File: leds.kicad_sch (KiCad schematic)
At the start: 32 parts

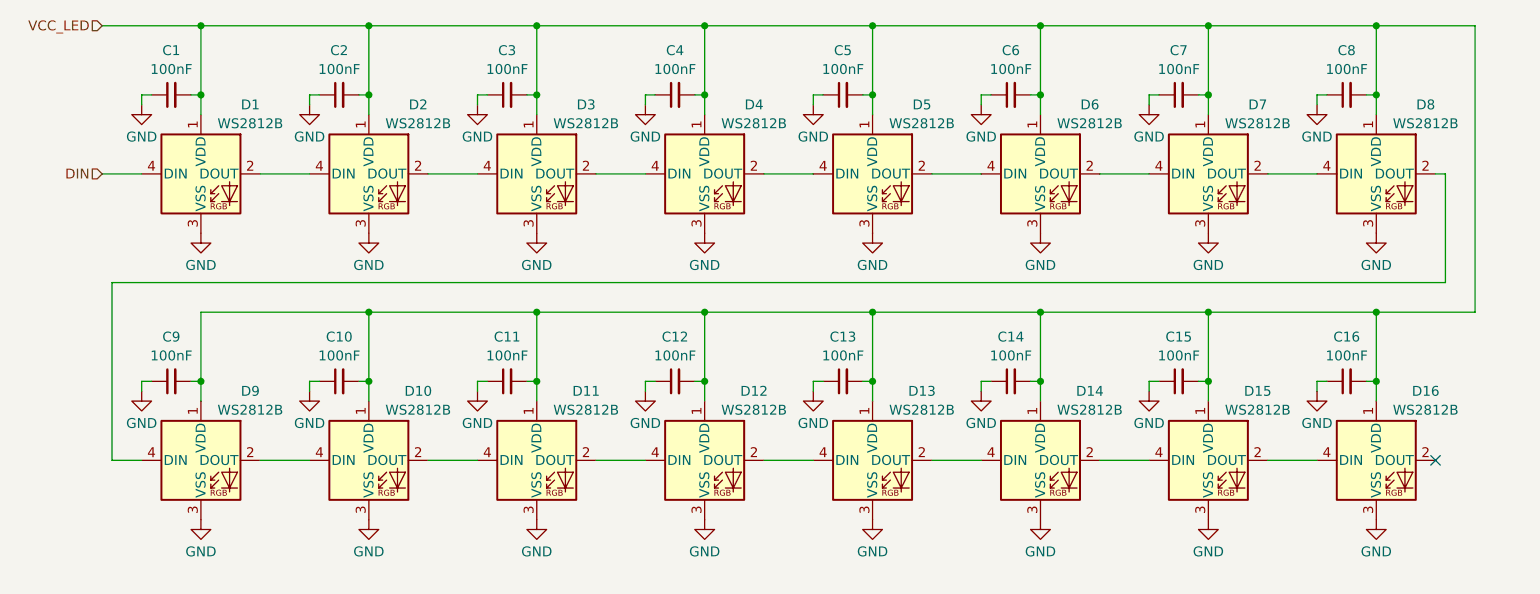
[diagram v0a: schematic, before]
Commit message: Finish rough layout
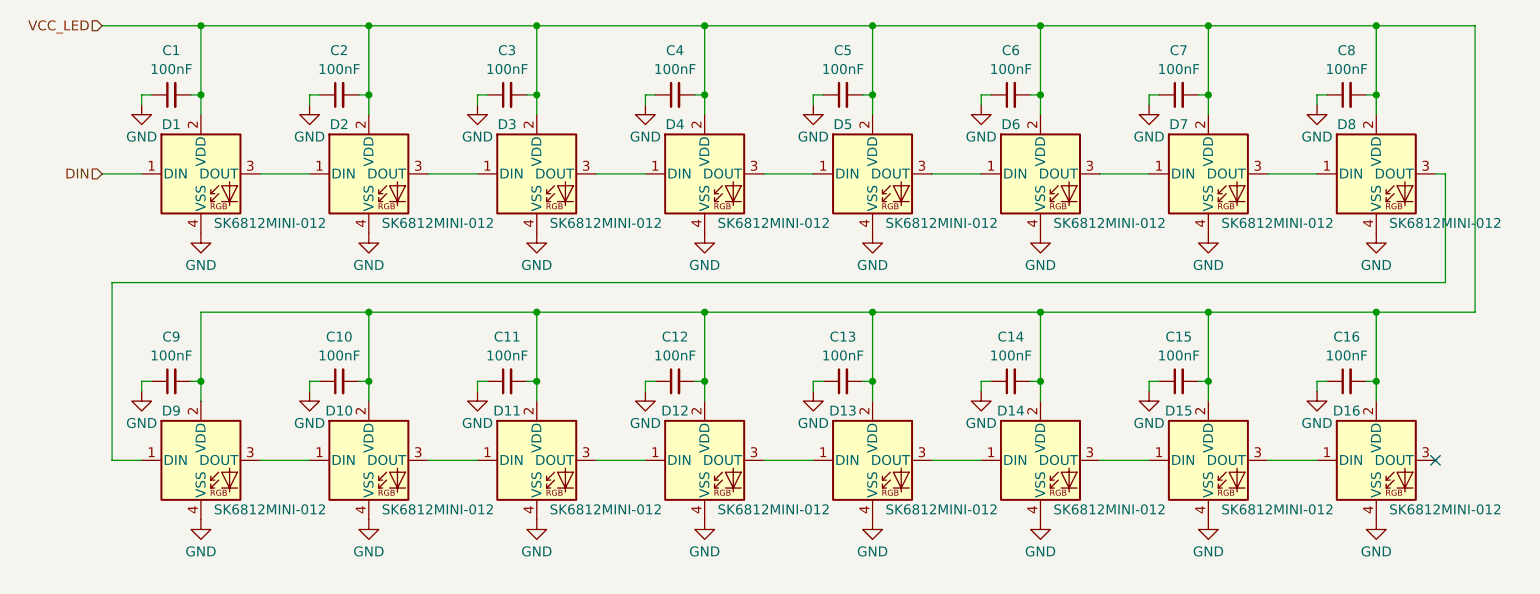
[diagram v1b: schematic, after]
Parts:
- removed D1, D10, D11, D12, D13, D14, D15, D16, D2, D3, D4, D5, D6, D7, D8, D9: WS2812B, LED_SMD:LED_SK6812MINI_PLCC4_3.5x3.5mm_P1.75mm, symbol LED:WS2812B
- added D1, D10, D11, D12, D13, D14, D15, D16, D2, D3, D4, D5, D6, D7, D8, D9: SK6812MINI-012, LED_SMD_RGB:XXXX12-X1, symbol LED_OPSCO:SK6812MINI-012
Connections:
- net DIN: now also D1.1 (DIN)
- net GND: now also D1.4 (VSS), D10.4 (VSS), D11.4 (VSS), D12.4 (VSS), D13.4 (VSS), D14.4 (VSS), D15.4 (VSS), D16.4 (VSS), D2.4 (VSS), D3.4 (VSS), D4.4 (VSS), D5.4 (VSS), D6.4 (VSS), D7.4 (VSS), D8.4 (VSS), D9.4 (VSS)
- net VCC_LED: now also D1.2 (VDD), D10.2 (VDD), D11.2 (VDD), D12.2 (VDD), D13.2 (VDD), D14.2 (VDD), D15.2 (VDD), D16.2 (VDD), D2.2 (VDD), D3.2 (VDD), D4.2 (VDD), D5.2 (VDD), D6.2 (VDD), D7.2 (VDD), D8.2 (VDD), D9.2 (VDD)
- new net: D5.3 (DOUT), D6.1 (DIN)
- new net: D6.3 (DOUT), D7.1 (DIN)
- new net: D1.3 (DOUT), D2.1 (DIN)
- new net: D12.3 (DOUT), D13.1 (DIN)
- new net: D13.3 (DOUT), D14.1 (DIN)
- new net: D2.3 (DOUT), D3.1 (DIN)
- new net: D3.3 (DOUT), D4.1 (DIN)
- new net: D10.1 (DIN), D9.3 (DOUT)
- new net: D10.3 (DOUT), D11.1 (DIN)
- new net: D11.3 (DOUT), D12.1 (DIN)
- new net: D4.3 (DOUT), D5.1 (DIN)
- new net: D8.3 (DOUT), D9.1 (DIN)
- new net: D14.3 (DOUT), D15.1 (DIN)
- new net: D7.3 (DOUT), D8.1 (DIN)
- new net: D15.3 (DOUT), D16.1 (DIN)

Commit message: Relayout board to fit constraints of Micro USB Blinkekatzen
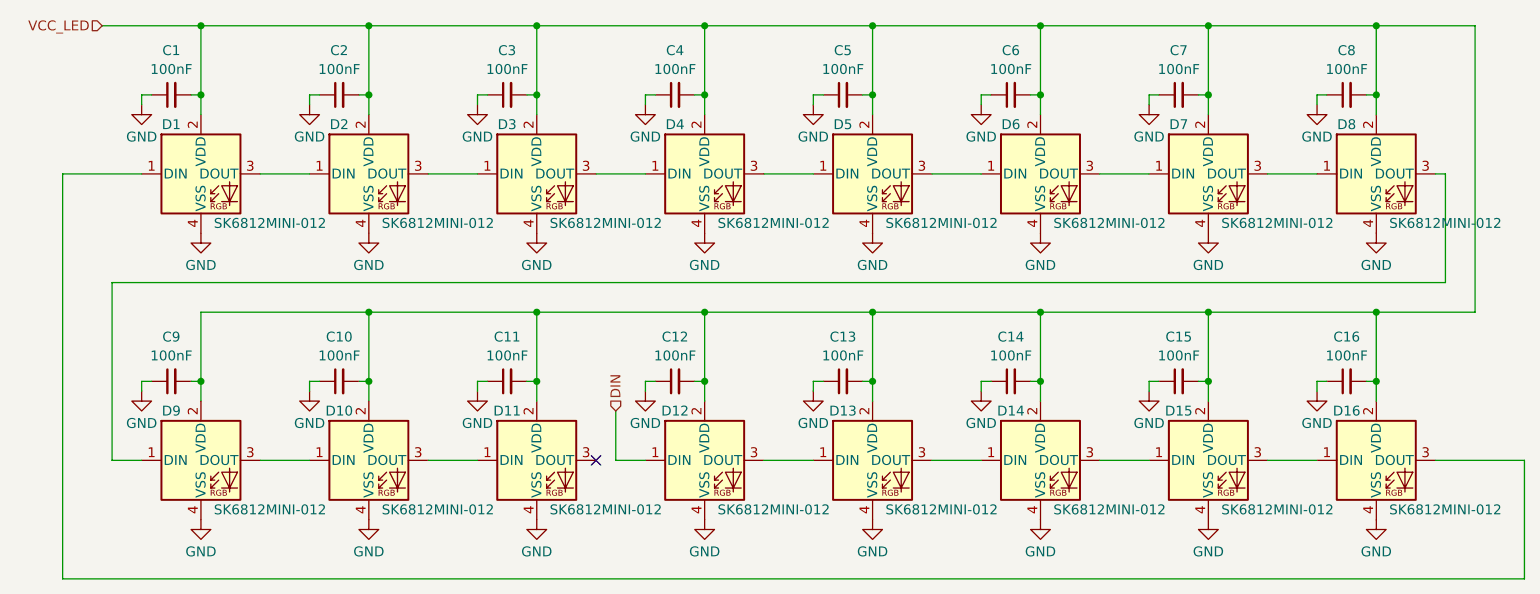
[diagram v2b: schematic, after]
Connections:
- net DIN: now also D12.1 (DIN); no longer D1.1 (DIN)
- net at D11.3 (DOUT): no longer D12.1 (DIN)
- net at D16.3 (DOUT): now also D1.1 (DIN)
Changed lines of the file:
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@@
   (junction (at 146.05 57.15) (diameter 0) (color 0 0 0 0)
   )
-  (no_connect (at 218.44 104.14))
+  (no_connect (at 110.49 104.14))
   (wire (pts (xy 209.55 93.98) (xy 210.82 93.98))
     (stroke (width 0) (type default))
@@
     (stroke (width 0) (type default))
   )
-  (wire (pts (xy 46.99 67.31) (xy 52.07 67.31))
+  (wire (pts (xy 41.91 67.31) (xy 52.07 67.31))
     (stroke (width 0) (type default))
   )
@@
     (stroke (width 0) (type default))
   )
+  (wire (pts (xy 113.03 104.14) (xy 116.84 104.14))
+    (stroke (width 0) (type default))
+  )
   (wire (pts (xy 210.82 93.98) (xy 210.82 85.09))
     (stroke (width 0) (type default))
@@
     (stroke (width 0) (type default))
   )
-  (wire (pts (xy 110.49 104.14) (xy 116.84 104.14))
-    (stroke (width 0) (type default))
-  )
   (wire (pts (xy 189.23 57.15) (xy 189.23 48.26))
     (stroke (width 0) (type default))
@@
     (stroke (width 0) (type default))
   )
+  (wire (pts (xy 229.87 119.38) (xy 41.91 119.38))
+    (stroke (width 0) (type default))
+  )
   (wire (pts (xy 46.99 48.26) (xy 59.69 48.26))
     (stroke (width 0) (type default))
@@
     (stroke (width 0) (type default))
   )
+  (wire (pts (xy 229.87 104.14) (xy 229.87 119.38))
+    (stroke (width 0) (type default))
+  )
   (wire (pts (xy 132.08 104.14) (xy 138.43 104.14))
     (stroke (width 0) (type default))
@@
     (stroke (width 0) (type default))
   )
+  (wire (pts (xy 113.03 97.79) (xy 113.03 104.14))
+    (stroke (width 0) (type default))
+  )
   (wire (pts (xy 81.28 93.98) (xy 81.28 96.52))
     (stroke (width 0) (type default))
@@
     (stroke (width 0) (type default))
   )
+  (wire (pts (xy 41.91 119.38) (xy 41.91 67.31))
+    (stroke (width 0) (type default))
+  )
   (wire (pts (xy 175.26 67.31) (xy 181.61 67.31))
     (stroke (width 0) (type default))
@@
     (stroke (width 0) (type default))
   )
+  (wire (pts (xy 218.44 104.14) (xy 229.87 104.14))
+    (stroke (width 0) (type default))
+  )
   (wire (pts (xy 153.67 104.14) (xy 160.02 104.14))
     (stroke (width 0) (type default))
@@
     (stroke (width 0) (type default))
   )
-  (hierarchical_label "DIN" (shape input) (at 46.99 67.31 180) (fields_autoplaced)
-    (effects (font (size 1.27 1.27)) (justify right))
+  (hierarchical_label "DIN" (shape input) (at 113.03 97.79 90) (fields_autoplaced)
+    (effects (font (size 1.27 1.27)) (justify left))
   )
   (hierarchical_label "VCC_LED" (shape input) (at 46.99 48.26 180) (fields_autoplaced)
